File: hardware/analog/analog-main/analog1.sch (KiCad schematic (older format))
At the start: 15 parts, among them K2 SANYOU_SRD_Form_C, Q2 2N2222, U13 LMV321, U14 LMV321, U15 OPA549, U16 74HCT04

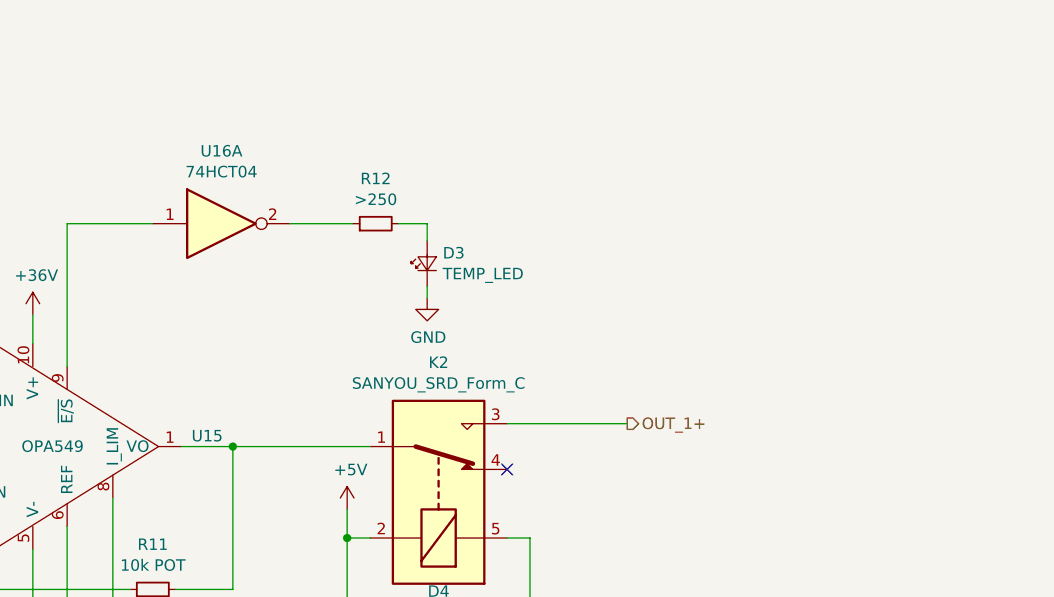
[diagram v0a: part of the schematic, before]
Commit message: Applied fixed symbol for OPA549
Configured all footprints
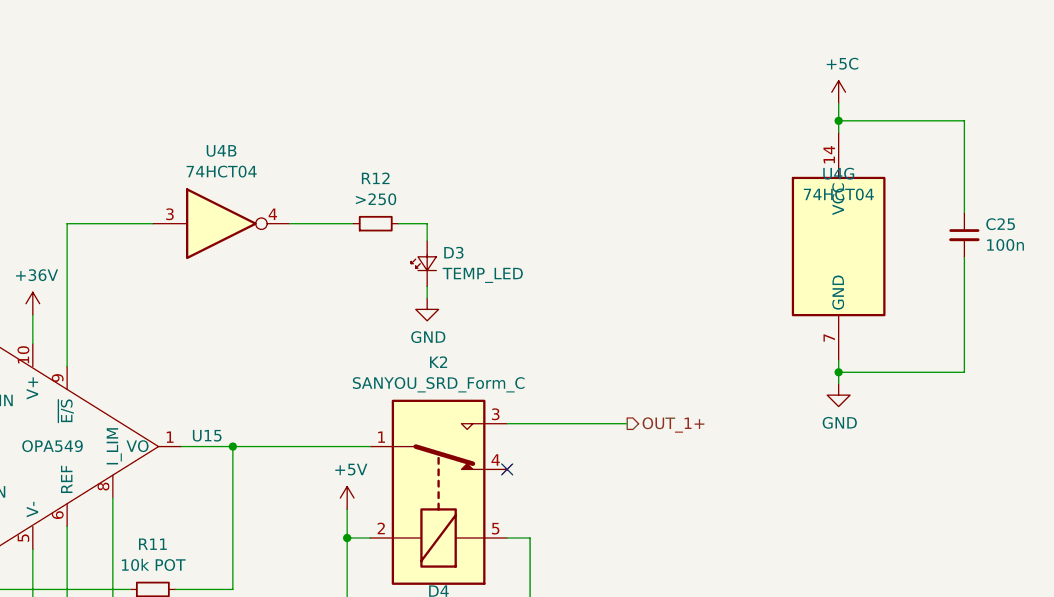
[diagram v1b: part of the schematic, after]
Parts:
- added C25: 100n, Capacitor_SMD:C_0603_1608Metric, symbol Device:C_Small
- added unit 7 of U4
- D3: footprint (none) -> LED_THT:LED_D5.0mm
- D4: footprint (none) -> Diode_THT:D_DO-35_SOD27_P7.62mm_Horizontal
- R11: footprint (none) -> Potentiometer_THT:Potentiometer_Bourns_3296W_Vertical
- renumbered U16 to U4
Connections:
- net +5C: now also C25.1, U4.14 (VCC)
- net GND: now also C25.2, U4.7 (GND)
- net at U15.9 (~E/S): now also U4.3; no longer U4.1
- net at R12.1: now also U4.4; no longer U4.2
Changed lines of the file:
@@
 $Comp
 L 74xx:74HCT04 U?
-U 1 1 5E9820B2
+U 2 1 5E9820B2
 P 4750 1425
 AR Path="/5E862B85/5E9820B2" Ref="U?"  Part="1"
 AR Path="/5E96F94C/5E9820B2" Ref="U?"  Part="1"
-AR Path="/5E975E66/5E9820B2" Ref="U16"  Part="1"
-F 0 "U16" H 4750 1742 50  0000 C CNN
+AR Path="/5E975E66/5E9820B2" Ref="U4"  Part="2"
+F 0 "U4" H 4750 1742 50  0000 C CNN
 F 1 "74HCT04" H 4750 1651 50  0000 C CNN
 F 2 "" H 4750 1425 50  0001 C CNN
 F 3 "https://assets.nexperia.com/documents/data-sheet/74HC_HCT04.pdf" H 4750 1425 50  0001 C CNN
-	1    4750 1425
+	2    4750 1425
 	1    0    0    -1
 $EndComp
@@
 F 0 "R11" V 4646 3025 50  0000 C CNN
 F 1 "10k POT" V 4555 3025 50  0000 C CNN
-F 2 "" H 4450 3025 50  0001 C CNN
+F 2 "Potentiometer_THT:Potentiometer_Bourns_3296W_Vertical" H 4450 3025 50  0001 C CNN
 F 3 "~" H 4450 3025 50  0001 C CNN
 	1    4450 3025
@@
 F 0 "D3" V 5696 1532 50  0000 R CNN
 F 1 "TEMP_LED" V 5605 1532 50  0000 R CNN
-F 2 "" V 5650 1600 50  0001 C CNN
+F 2 "LED_THT:LED_D5.0mm" V 5650 1600 50  0001 C CNN
 F 3 "~" V 5650 1600 50  0001 C CNN
 	1    5650 1600
@@
 F 0 "D4" H 5700 3466 50  0000 C CNN
 F 1 "D_Zener" H 5700 3375 50  0000 C CNN
-F 2 "" H 5700 3250 50  0001 C CNN
+F 2 "Diode_THT:D_DO-35_SOD27_P7.62mm_Horizontal" H 5700 3250 50  0001 C CNN
 F 3 "~" H 5700 3250 50  0001 C CNN
 	1    5700 3250
@@
 Text HLabel 6525 2300 2    50   Output ~ 0
 OUT_1+
+$Comp
+L 74xx:74HCT04 U?
+U 7 1 5EAC3E32
+P 7450 1525
+AR Path="/5E862B85/5EAC3E32" Ref="U?"  Part="1"
+AR Path="/5E96F94C/5EAC3E32" Ref="U?"  Part="1"
+AR Path="/5E975E66/5EAC3E32" Ref="U4"  Part="7"
+F 0 "U4" H 7450 1842 50  0000 C CNN
+F 1 "74HCT04" H 7450 1751 50  0000 C CNN
+F 2 "" H 7450 1525 50  0001 C CNN
+F 3 "https://assets.nexperia.com/documents/data-sheet/74HC_HCT04.pdf" H 7450 1525 50  0001 C CNN
+	7    7450 1525
+	1    0    0    -1
+$EndComp
+$Comp
+L Device:C_Small C?
+U 1 1 5EAC8AF7
+P 8000 1475
+AR Path="/5E862B85/5EAC8AF7" Ref="C?"  Part="1"
+AR Path="/5E96F94C/5EAC8AF7" Ref="C?"  Part="1"
+AR Path="/5E975E66/5EAC8AF7" Ref="C25"  Part="1"
+F 0 "C25" H 8092 1521 50  0000 L CNN
+F 1 "100n" H 8092 1430 50  0000 L CNN
+F 2 "Capacitor_SMD:C_0603_1608Metric" H 8000 1475 50  0001 C CNN
+F 3 "~" H 8000 1475 50  0001 C CNN
+	1    8000 1475
+	1    0    0    -1
+$EndComp
+Wire Wire Line
+	8000 1375 8000 975
+Wire Wire Line
+	8000 975  7450 975
+Wire Wire Line
+	7450 975  7450 1025
+Wire Wire Line
+	7450 2025 7450 2075
+Wire Wire Line
+	7450 2075 8000 2075
+Wire Wire Line
+	8000 2075 8000 1575
+$Comp
+L power:+5C #PWR?
+U 1 1 5EACF7FB
+P 7450 900
+AR Path="/5E862B85/5EACF7FB" Ref="#PWR?"  Part="1"
+AR Path="/5E96F94C/5EACF7FB" Ref="#PWR?"  Part="1"
+AR Path="/5E975E66/5EACF7FB" Ref="#PWR0101"  Part="1"
+F 0 "#PWR0101" H 7450 750 50  0001 C CNN
+F 1 "+5C" H 7465 1073 50  0000 C CNN
+F 2 "" H 7450 900 50  0001 C CNN
+F 3 "" H 7450 900 50  0001 C CNN
+	1    7450 900
+	1    0    0    -1
+$EndComp
+Wire Wire Line
+	7450 900  7450 975
+Connection ~ 7450 975
+$Comp
+L power:GND #PWR0102
+U 1 1 5EAD2C37
+P 7450 2125
+F 0 "#PWR0102" H 7450 1875 50  0001 C CNN
+F 1 "GND" H 7455 1952 50  0000 C CNN
+F 2 "" H 7450 2125 50  0001 C CNN
+F 3 "" H 7450 2125 50  0001 C CNN
+	1    7450 2125
+	1    0    0    -1
+$EndComp
+Wire Wire Line
+	7450 2125 7450 2075
+Connection ~ 7450 2075
 $EndSCHEMATC

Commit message: Sorry future me
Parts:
- added C35: 4700u, Capacitor_THT:CP_Radial_D26.0mm_P10.00mm_SnapIn, symbol Device:CP
- added R?: 100R 1W+, Resistor_SMD:R_0603_1608Metric, symbol Device:R_Small
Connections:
- net GND: now also C35.2, R?.1
- net at K2.1, R11.2, U15.1 (VO)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: now also C35.1
- net at K2.4: now also R?.2
- net +36V renamed V+
- no-connect marks 1 -> 0
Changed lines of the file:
@@
 $Descr A4 11693 8268
 encoding utf-8
-Sheet 5 6
+Sheet 5 7
 Title ""
 Date ""
@@
 Connection ~ 1725 800
 $Comp
-L power:+36V #PWR?
-U 1 1 5E98216B
-P 3925 1825
-AR Path="/5E862B85/5E98216B" Ref="#PWR?"  Part="1"
-AR Path="/5E96F94C/5E98216B" Ref="#PWR?"  Part="1"
-AR Path="/5E975E66/5E98216B" Ref="#PWR045"  Part="1"
-F 0 "#PWR045" H 3925 1675 50  0001 C CNN
-F 1 "+36V" H 3940 1998 50  0000 C CNN
-F 2 "" H 3925 1825 50  0001 C CNN
-F 3 "" H 3925 1825 50  0001 C CNN
-	1    3925 1825
-	1    0    0    -1
-$EndComp
-$Comp
 L Relay:SANYOU_SRD_Form_C K?
 U 1 1 5E982171
@@
 $EndComp
 Wire Wire Line
-	5400 2400 4800 2400
+	5400 2400 5025 2400
 Connection ~ 4800 2400
 $Comp
@@
 	1    0    0    -1
 $EndComp
-NoConn ~ 6000 2500
 $Comp
 L Device:D_Zener D?
@@
 	7450 2125 7450 2075
 Connection ~ 7450 2075
+$Comp
+L Device:CP C?
+U 1 1 5EBD65F9
+P 5025 2625
+AR Path="/5EBAB32F/5EBD65F9" Ref="C?"  Part="1"
+AR Path="/5E975E66/5EBD65F9" Ref="C35"  Part="1"
+F 0 "C35" H 5143 2671 50  0000 L CNN
+F 1 "4700u" H 5143 2580 50  0000 L CNN
+F 2 "Capacitor_THT:CP_Radial_D26.0mm_P10.00mm_SnapIn" H 5063 2475 50  0001 C CNN
+F 3 "~" H 5025 2625 50  0001 C CNN
+	1    5025 2625
+	1    0    0    -1
+$EndComp
+$Comp
+L power:GND #PWR?
+U 1 1 5EBD8342
+P 5025 2850
+AR Path="/5E862B85/5EBD8342" Ref="#PWR?"  Part="1"
+AR Path="/5E96F94C/5EBD8342" Ref="#PWR?"  Part="1"
+AR Path="/5E975E66/5EBD8342" Ref="#PWR0110"  Part="1"
+F 0 "#PWR0110" H 5025 2600 50  0001 C CNN
+F 1 "GND" H 5030 2677 50  0000 C CNN
+F 2 "" H 5025 2850 50  0001 C CNN
+F 3 "" H 5025 2850 50  0001 C CNN
+	1    5025 2850
+	1    0    0    -1
+$EndComp
+Wire Wire Line
+	5025 2850 5025 2775
+Text Label 3925 1825 2    50   ~ 0
+AN1_VCC
+$Comp
+L Device:R_Small R?
+U 1 1 5EC01140
+P 6225 2500
+AR Path="/5E862B85/5EC01140" Ref="R?"  Part="1"
+AR Path="/5E96F94C/5EC01140" Ref="R?"  Part="1"
+F 0 "R?" V 6029 2500 50  0000 C CNN
+F 1 "100R 1W+" V 6120 2500 50  0000 C CNN
+F 2 "Resistor_SMD:R_0603_1608Metric" H 6225 2500 50  0001 C CNN
+F 3 "~" H 6225 2500 50  0001 C CNN
+	1    6225 2500
+	0    1    1    0
+$EndComp
+Wire Wire Line
+	6125 2500 6000 2500
+$Comp
+L power:GND #PWR?
+U 1 1 5EC01147
+P 6425 2575
+F 0 "#PWR?" H 6425 2325 50  0001 C CNN
+F 1 "GND" H 6430 2402 50  0000 C CNN
+F 2 "" H 6425 2575 50  0001 C CNN
+F 3 "" H 6425 2575 50  0001 C CNN
+	1    6425 2575
+	1    0    0    -1
+$EndComp
+Wire Wire Line
+	6425 2575 6425 2500
+Wire Wire Line
+	6425 2500 6325 2500
+Wire Wire Line
+	5025 2475 5025 2400
+Connection ~ 5025 2400
+Wire Wire Line
+	5025 2400 4800 2400
 $EndSCHEMATC
